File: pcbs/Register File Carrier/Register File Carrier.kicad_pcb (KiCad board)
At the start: 2 copper layers, 236.2 x 205.7 mm, 96 parts, among them J1001 Conn_02x20_Odd_Even, J1002 Conn_02x20_Odd_Even, U2001 74AHC04, U3001 74HC14, U3002 74HC08, U3003 74HC138, U3004 74HC08

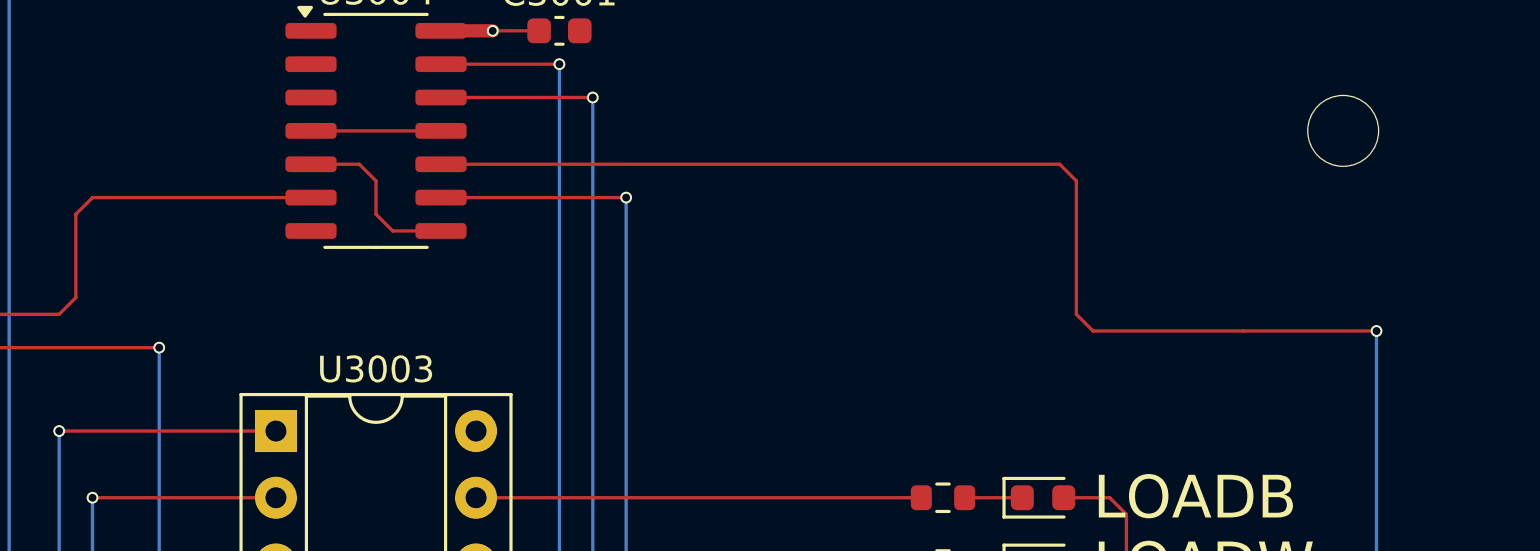
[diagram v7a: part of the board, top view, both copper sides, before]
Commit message: Add Active indicator
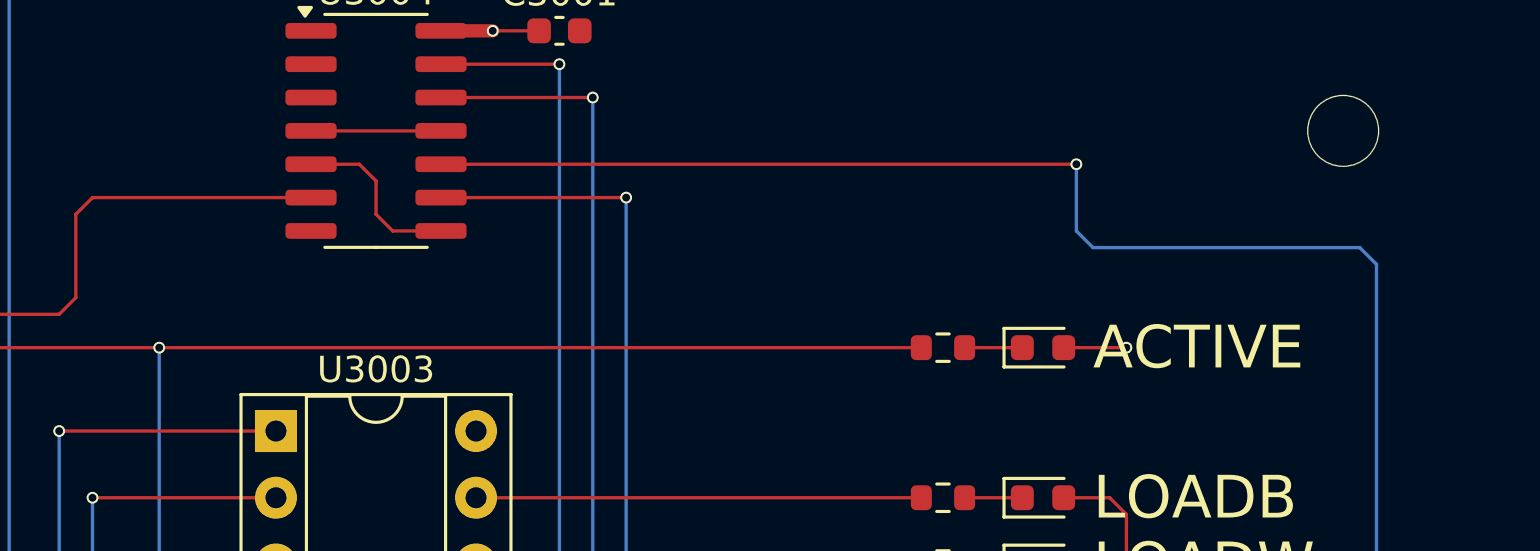
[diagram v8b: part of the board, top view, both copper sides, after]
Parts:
- added D3009: Blue, LED_SMD:LED_0603_1608Metric, F.Cu at (278.1, 64.1)
- added R3009: 4k7, Resistor_SMD:R_0603_1608Metric, F.Cu at (274.3, 64.1)
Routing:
- net /Connector Block/~{Active}: track 298.9 -> 328.0 mm
- net +5V: track 46.4 -> 48.8 mm, vias 10 -> 11
- net Net-(D3009-K): track 0.00 -> 2.20 mm
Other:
- board text added: "ACTIVE"
